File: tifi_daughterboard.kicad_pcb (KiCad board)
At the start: 2 copper layers, 57.4 x 32.3 mm, 19 parts, among them J1 SSW-110-23-F-D, J2 SSW-110-23-F-D, J3 SM04B-SRSS-TB(LF)(SN), J4 SSW-103-02-T-S-RA, Q1 BSS138LT1G, U1 SGP40-D-R4, U2 SHT40-AD1B-R3

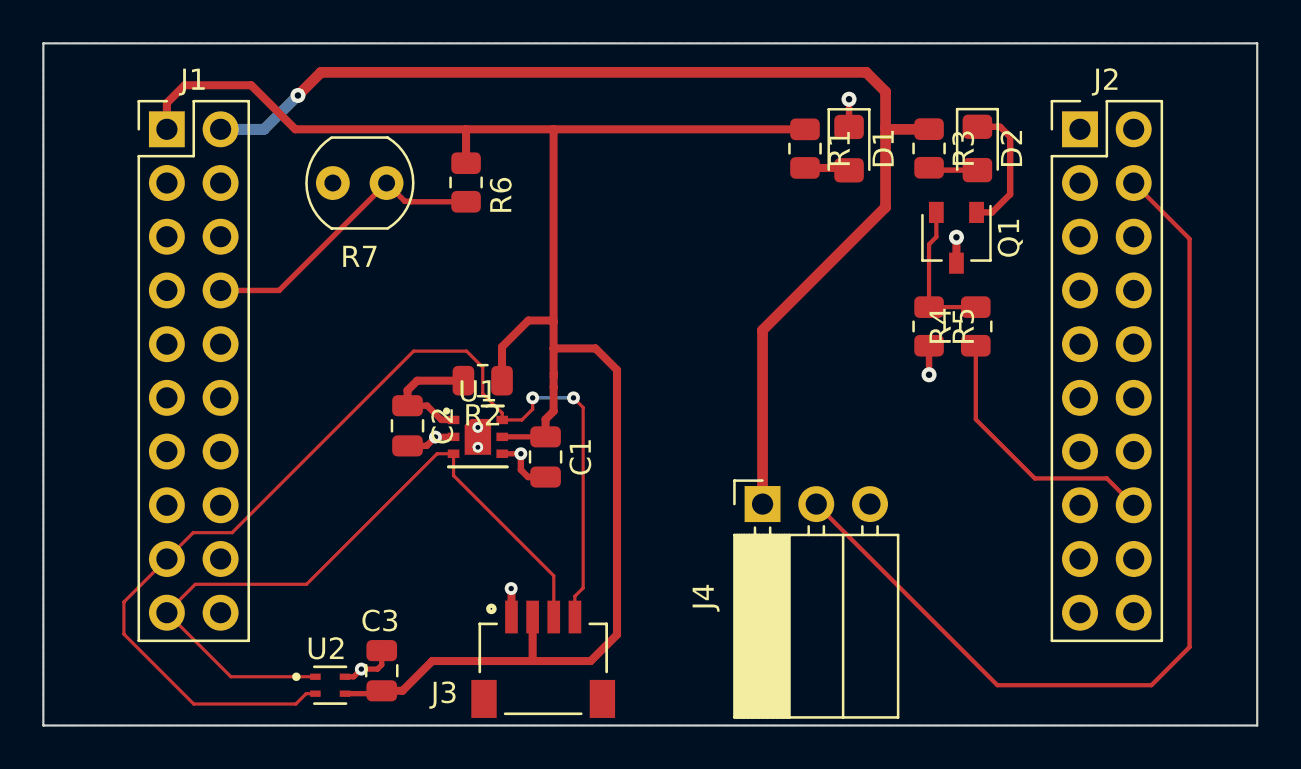
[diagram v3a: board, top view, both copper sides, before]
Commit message: Add alignment silkscreen.
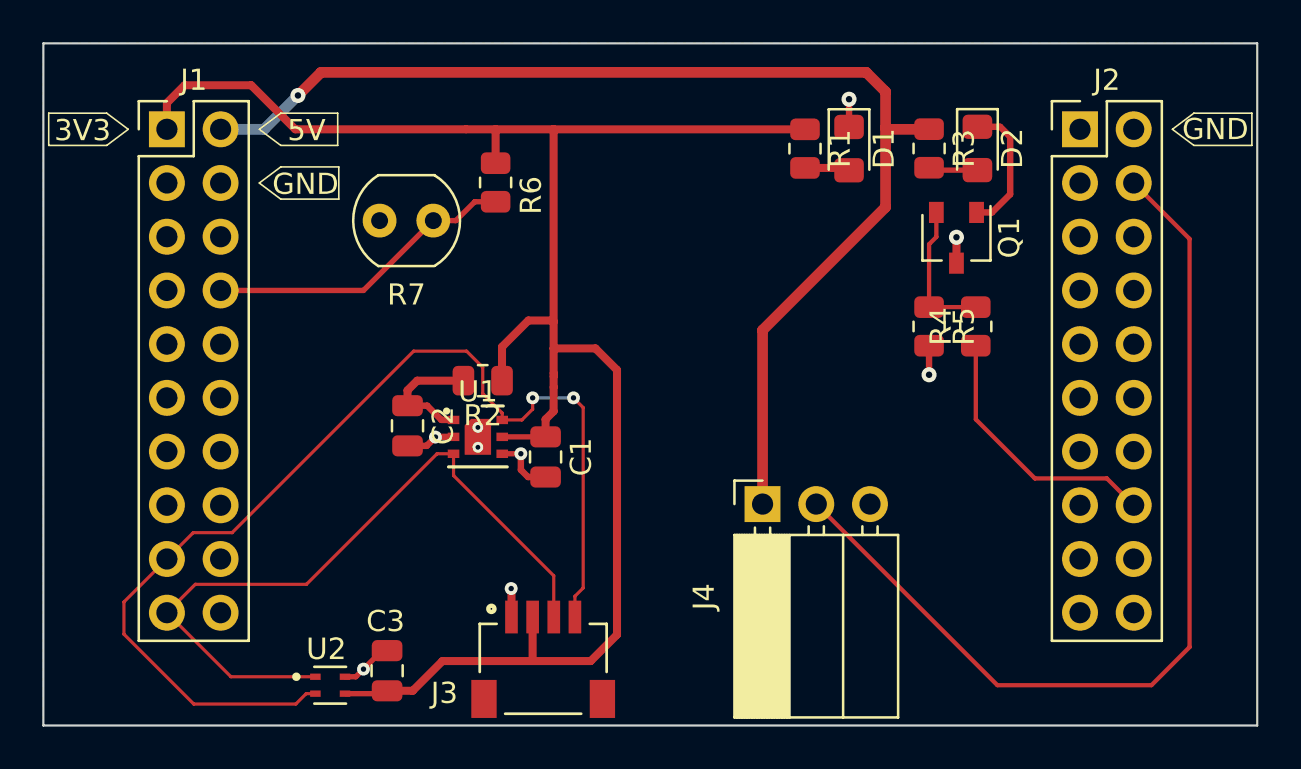
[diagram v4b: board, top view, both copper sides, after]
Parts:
- moved R7 2.84 mm to (134.5, 78.0)
- moved R6 1.40 mm to (137.5, 76.2)
- moved C3 0.25 mm to (132.3, 99.3)
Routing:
- net LDR_OUT: track 14.1 -> 14.7 mm
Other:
- board text added: "3V3"
- board text added: "5V"
- board text added: "GND"
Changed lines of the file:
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@@
     )
     (pad_to_mask_clearance 0)
+    (grid_origin 133.5532 99.822)
     (pcbplotparams
       (layerselection 0x00010fc_ffffffff)
@@
   )
   (footprint "OptoDevice:R_LDR_4.9x4.2mm_P2.54mm_Vertical" (layer "F.Cu")
-    (at 132.3086 76.2 180)
+    (at 134.5184 77.978 180)
     (descr "Resistor, LDR 4.9x4.2mm")
     (tags "Resistor LDR4.9x4.2")
@@
   )
   (footprint "Capacitor_SMD:C_0805_2012Metric" (layer "F.Cu")
-    (at 132.08 99.2632 90)
+    (at 132.334 99.2632 90)
     (descr "Capacitor SMD 0805 (2012 Metric), square (rectangular) end terminal, IPC_7351 nominal, (Body size source: IPC-SM-782 page 76, https://www.pcb-3d.com/wordpress/wp-content/uploads/ipc-sm-782a_amendment_1_and_2.pdf, https://docs.google.com/spreadsheets/d/1BsfQQcO9C6DZCsRaXUlFlo91Tg2WpOkGARC1WS5S8t0/edit?usp=sharing), generated with kicad-footprint-generator")
     (tags "capacitor")
@@
   )
   (footprint "Resistor_SMD:R_0805_2012Metric" (layer "F.Cu")
-    (at 136.0678 76.1746 -90)
+    (at 137.4648 76.1746 -90)
     (descr "Resistor SMD 0805 (2012 Metric), square (rectangular) end terminal, IPC_7351 nominal, (Body size source: IPC-SM-782 page 72, https://www.pcb-3d.com/wordpress/wp-content/uploads/ipc-sm-782a_amendment_1_and_2.pdf), generated with kicad-footprint-generator")
     (tags "resistor")
@@
     )
   )
+  (gr_poly
+    (pts
+      (xy 120.0912 73.66)
+      (xy 119.0752 74.422)
+      (xy 116.332 74.422)
+      (xy 116.332 72.898)
+      (xy 119.0752 72.898)
+    ) (layer "F.SilkS") (width 0.0762) (fill none))
+  (gr_poly
+    (pts
+      (xy 169.4688 73.66)
+      (xy 170.4848 72.898)
+      (xy 173.228 72.898)
+      (xy 173.228 74.422)
+      (xy 170.4848 74.422)
+    ) (layer "F.SilkS") (width 0.0762) (fill none))
+  (gr_poly
+    (pts
+      (xy 126.2888 76.2)
+      (xy 127.3048 75.438)
+      (xy 130.048 75.438)
+      (xy 130.048 76.962)
+      (xy 127.3048 76.962)
+    ) (layer "F.SilkS") (width 0.0762) (fill none))
+  (gr_poly
+    (pts
+      (xy 126.2888 73.66)
+      (xy 127.3048 72.898)
+      (xy 129.9972 72.898)
+      (xy 129.9972 74.422)
+      (xy 127.3048 74.422)
+    ) (layer "F.SilkS") (width 0.0762) (fill none))
   (gr_rect (start 116.078 69.596) (end 173.482 101.854) (layer "Edge.Cuts") (width 0.1016) (fill none))
-  (segment (start 139.2682 98.806) (end 134.4676 98.806) (width 0.381) (layer "F.Cu") (net 1))
+  (gr_text "GND" (at 128.4732 76.2508) (layer "F.SilkS")
+    (effects (font (size 1 1) (thickness 0.15)))
+  )
+  (gr_text "GND" (at 171.5008 73.66) (layer "F.SilkS")
+    (effects (font (size 1 1) (thickness 0.15)))
+  )
+  (gr_text "3V3" (at 117.9322 73.7108) (layer "F.SilkS")
+    (effects (font (size 1 1) (thickness 0.15)))
+  )
+  (gr_text "5V" (at 128.524 73.7108) (layer "F.SilkS")
+    (effects (font (size 1 1) (thickness 0.15)))
+  )
   (segment (start 140.208 85.852) (end 140.208 86.995) (width 0.381) (layer "F.Cu") (net 1))
   (segment (start 137.7677 85.5472) (end 137.7677 83.9489) (width 0.381) (layer "F.Cu") (net 1))
@@
   (segment (start 139.827 87.376) (end 139.827 88.204) (width 0.381) (layer "F.Cu") (net 1))
   (segment (start 139.2682 98.806) (end 139.215 98.7528) (width 0.381) (layer "F.Cu") (net 1))
-  (segment (start 136.0678 75.2621) (end 136.0678 73.66) (width 0.381) (layer "F.Cu") (net 1))
   (segment (start 139.215 98.7528) (end 139.215 96.7232) (width 0.381) (layer "F.Cu") (net 1))
+  (segment (start 140.208 73.66) (end 137.4648 73.66) (width 0.381) (layer "F.Cu") (net 1))
   (segment (start 139.0142 82.7024) (end 140.1572 82.7024) (width 0.381) (layer "F.Cu") (net 1))
+  (segment (start 137.4648 73.66) (end 136.0678 73.66) (width 0.381) (layer "F.Cu") (net 1))
   (segment (start 143.2052 97.5614) (end 141.9606 98.806) (width 0.381) (layer "F.Cu") (net 1))
-  (segment (start 133.0604 100.2132) (end 132.08 100.2132) (width 0.381) (layer "F.Cu") (net 1))
   (segment (start 140.208 84.0232) (end 142.1892 84.0232) (width 0.381) (layer "F.Cu") (net 1))
-  (segment (start 131.9442 100.349) (end 132.08 100.2132) (width 0.254) (layer "F.Cu") (net 1))
+  (segment (start 132.1322 100.349) (end 132.268 100.2132) (width 0.254) (layer "F.Cu") (net 1))
+  (segment (start 134.9502 98.806) (end 139.2682 98.806) (width 0.381) (layer "F.Cu") (net 1))
+  (segment (start 137.4648 75.2621) (end 137.4648 73.66) (width 0.381) (layer "F.Cu") (net 1))
   (segment (start 127.9906 73.66) (end 136.0678 73.66) (width 0.381) (layer "F.Cu") (net 1))
   (segment (start 142.1892 84.0232) (end 143.2052 85.0392) (width 0.381) (layer "F.Cu") (net 1))
   (segment (start 137.7677 83.9489) (end 139.0142 82.7024) (width 0.381) (layer "F.Cu") (net 1))
   (segment (start 140.208 85.344) (end 140.208 85.852) (width 0.381) (layer "F.Cu") (net 1))
+  (segment (start 133.543 100.2132) (end 134.9502 98.806) (width 0.381) (layer "F.Cu") (net 1))
   (segment (start 121.92 73.66) (end 121.92 72.4154) (width 0.381) (layer "F.Cu") (net 1))
+  (segment (start 132.268 100.2132) (end 133.543 100.2132) (width 0.381) (layer "F.Cu") (net 1))
   (segment (start 140.208 85.1916) (end 140.208 85.344) (width 0.381) (layer "F.Cu") (net 1))
   (segment (start 140.208 84.0232) (end 140.208 85.1916) (width 0.381) (layer "F.Cu") (net 1))
@@
   (segment (start 143.2052 85.0392) (end 143.2052 97.5614) (width 0.381) (layer "F.Cu") (net 1))
   (segment (start 137.7766 88.204) (end 139.827 88.204) (width 0.254) (layer "F.Cu") (net 1))
-  (segment (start 140.208 73.66) (end 136.0678 73.66) (width 0.381) (layer "F.Cu") (net 1))
   (segment (start 130.3416 100.349) (end 131.9442 100.349) (width 0.254) (layer "F.Cu") (net 1))
   (segment (start 140.2095 73.6615) (end 140.208 73.66) (width 0.381) (layer "F.Cu") (net 1))
   (segment (start 140.208 86.995) (end 139.827 87.376) (width 0.381) (layer "F.Cu") (net 1))
-  (segment (start 134.4676 98.806) (end 133.0604 100.2132) (width 0.381) (layer "F.Cu") (net 1))
   (segment (start 140.208 82.7532) (end 140.208 73.66) (width 0.381) (layer "F.Cu") (net 1))
   (segment (start 138.215 95.4668) (end 138.215 96.7232) (width 0.381) (layer "F.Cu") (net 2))
   (segment (start 137.7766 89.004) (end 138.6562 89.004) (width 0.254) (layer "F.Cu") (net 2))
   (segment (start 134.6302 88.204) (end 134.62 88.2142) (width 0.3048) (layer "F.Cu") (net 2))
-  (segment (start 131.1148 99.187) (end 131.8768 99.187) (width 0.254) (layer "F.Cu") (net 2))
   (segment (start 138.6586 89.7636) (end 138.999 90.104) (width 0.3048) (layer "F.Cu") (net 2))
-  (segment (start 131.8768 99.187) (end 132.08 98.9838) (width 0.254) (layer "F.Cu") (net 2))
+  (segment (start 130.8544 99.549) (end 130.3416 99.549) (width 0.254) (layer "F.Cu") (net 2))
   (segment (start 138.2014 95.4532) (end 138.215 95.4668) (width 0.381) (layer "F.Cu") (net 2))
   (segment (start 138.6562 89.004) (end 138.6586 89.0016) (width 0.254) (layer "F.Cu") (net 2))
-  (segment (start 130.7528 99.549) (end 131.1148 99.187) (width 0.254) (layer "F.Cu") (net 2))
-  (segment (start 130.3416 99.549) (end 130.7528 99.549) (width 0.254) (layer "F.Cu") (net 2))
+  (segment (start 131.2164 99.187) (end 130.8544 99.549) (width 0.254) (layer "F.Cu") (net 2))
   (segment (start 159.258 78.7654) (end 159.258 79.9908) (width 0.381) (layer "F.Cu") (net 2))
   (segment (start 157.9626 85.2678) (end 157.9626 83.8943) (width 0.3048) (layer "F.Cu") (net 2))
   (segment (start 135.4766 88.204) (end 134.6302 88.204) (width 0.3048) (layer "F.Cu") (net 2))
+  (segment (start 132.334 98.3132) (end 132.0902 98.3132) (width 0.254) (layer "F.Cu") (net 2))
   (segment (start 138.999 90.104) (end 139.827 90.104) (width 0.3048) (layer "F.Cu") (net 2))
   (segment (start 134.2034 88.6308) (end 134.62 88.2142) (width 0.3048) (layer "F.Cu") (net 2))
@@
   (segment (start 138.6586 89.0016) (end 138.6586 89.7636) (width 0.3048) (layer "F.Cu") (net 2))
   (segment (start 133.2992 88.6308) (end 134.2034 88.6308) (width 0.3048) (layer "F.Cu") (net 2))
-  (segment (start 132.08 98.9838) (end 132.08 98.3132) (width 0.254) (layer "F.Cu") (net 2))
-  (via (at 131.1148 99.187) (size 0.6096) (drill 0.254) (layers "F.Cu" "B.Cu") (free) (net 2))
+  (segment (start 132.0902 98.3132) (end 131.2164 99.187) (width 0.254) (layer "F.Cu") (net 2))
+  (via (at 131.2164 99.187) (size 0.6096) (drill 0.254) (layers "F.Cu" "B.Cu") (free) (net 2))
   (via (at 154.178 72.2376) (size 0.7112) (drill 0.3048) (layers "F.Cu" "B.Cu") (free) (net 2))
   (via (at 157.9626 85.2678) (size 0.7112) (drill 0.3048) (layers "F.Cu" "B.Cu") (free) (net 2))
@@
   (segment (start 126.5174 73.66) (end 124.46 73.66) (width 0.508) (layer "B.Cu") (net 6))
   (segment (start 128.1176 72.0598) (end 126.5174 73.66) (width 0.508) (layer "B.Cu") (net 6))
-  (segment (start 132.3086 76.2) (end 127.2286 81.28) (width 0.254) (layer "F.Cu") (net 11))
-  (segment (start 136.0678 77.0871) (end 133.4497 77.0871) (width 0.254) (layer "F.Cu") (net 11))
-  (segment (start 133.1722 77.0636) (end 132.3086 76.2) (width 0.254) (layer "F.Cu") (net 11))
-  (segment (start 127.2286 81.28) (end 124.46 81.28) (width 0.254) (layer "F.Cu") (net 11))
-  (segment (start 133.4497 77.0871) (end 133.4262 77.0636) (width 0.254) (layer "F.Cu") (net 11))
-  (segment (start 133.4262 77.0636) (end 133.1722 77.0636) (width 0.254) (layer "F.Cu") (net 11))
+  (segment (start 136.4761 77.0871) (end 135.5852 77.978) (width 0.254) (layer "F.Cu") (net 11))
+  (segment (start 137.4648 77.0871) (end 136.4761 77.0871) (width 0.254) (layer "F.Cu") (net 11))
+  (segment (start 135.5852 77.978) (end 134.5184 77.978) (width 0.254) (layer "F.Cu") (net 11))
+  (segment (start 134.5184 77.978) (end 131.2164 81.28) (width 0.254) (layer "F.Cu") (net 11))
+  (segment (start 131.2164 81.28) (end 124.46 81.28) (width 0.254) (layer "F.Cu") (net 11))
   (segment (start 170.2816 98.1456) (end 170.2816 78.8416) (width 0.2032) (layer "F.Cu") (net 12))
   (segment (start 170.2816 78.8416) (end 167.64 76.2) (width 0.2032) (layer "F.Cu") (net 12))

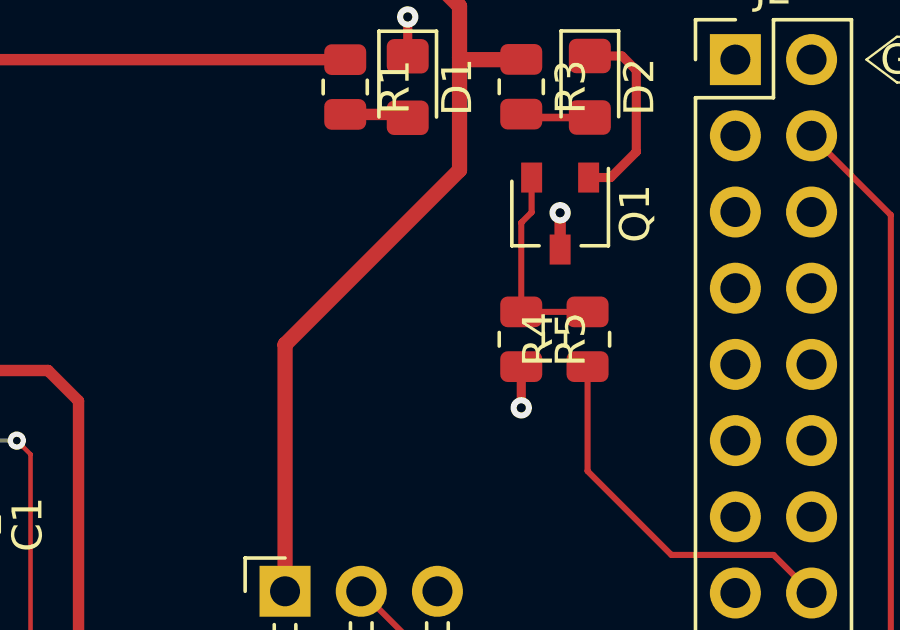
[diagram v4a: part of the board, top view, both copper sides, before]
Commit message: Add testpoint for LED driver FET gate.
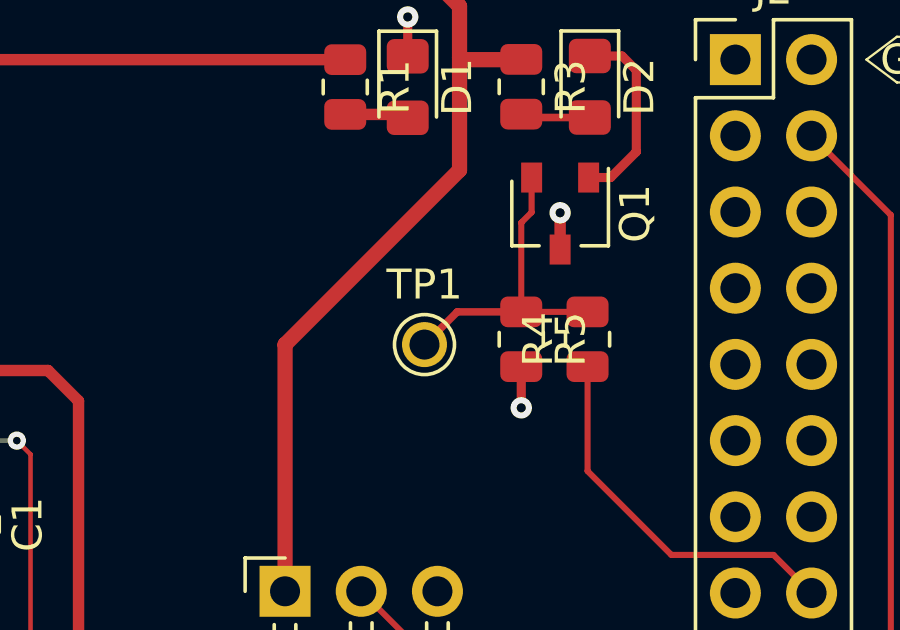
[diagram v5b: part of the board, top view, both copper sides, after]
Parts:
- added TP1: TestPoint, TiFi Footprints:TestPoint_THTPad_D1.5mm_Drill1.0mm, F.Cu at (154.7, 83.2)
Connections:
- U1 pad 7: GND -> (no net)
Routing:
- net Net-(Q1-Pad2): track 6.83 -> 10.5 mm
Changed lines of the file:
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@@
       (net 20 "I2C_SCL") (pinfunction "SCL") (pintype "input"))
     (pad "7" smd roundrect (at 0 0) (size 1.25 1.7) (layers "F.Cu" "F.Mask") (roundrect_rratio 0)
-      (chamfer_ratio 0.24) (chamfer top_left)
-      (net 2 "GND"))
+      (chamfer_ratio 0.24) (chamfer top_left))
     (model "${KICAD6_3DMODEL_DIR}/Package_DFN_QFN.3dshapes/DFN-6-1EP_2x2mm_P0.5mm_EP0.61x1.42mm.wrl" hide
       (offset (xyz 0 0 0))
@@
       (rotate (xyz -90 0 0))
     )
+  )
+  (footprint "TiFi Footprints:TestPoint_THTPad_D1.5mm_Drill1.0mm" (layer "F.Cu")
+    (at 154.7368 83.1596)
+    (descr "THT pad as test Point, diameter 2.0mm, hole diameter 1.0mm")
+    (tags "test point THT pad")
+    (property "Sheetfile" "tifi_daughterboard.kicad_sch")
+    (property "Sheetname" "")
+    (attr exclude_from_pos_files)
+    (fp_text reference "TP1" (at 0 -1.998) (layer "F.SilkS")
+      (effects (font (size 1 1) (thickness 0.15)))
+    )
+    (fp_text value "TestPoint" (at 0 2.05) (layer "F.Fab")
+      (effects (font (size 1 1) (thickness 0.15)))
+    )
+    (fp_text user "${REFERENCE}" (at 0 -2) (layer "F.Fab")
+      (effects (font (size 1 1) (thickness 0.15)))
+    )
+    (fp_circle (center 0 0) (end 1 0) (layer "F.SilkS") (width 0.12) (fill none))
+    (fp_circle (center 0 0) (end 1.3 0) (layer "F.CrtYd") (width 0.05) (fill none))
+    (pad "1" thru_hole circle (at 0 0) (size 1.5 1.5) (drill 1) (layers *.Cu *.Mask)
+      (net 42 "Net-(Q1-Pad2)") (pinfunction "1") (pintype "passive"))
   )
   (footprint "Capacitor_SMD:C_0805_2012Metric" (layer "F.Cu")
@@
   (segment (start 162.9664 90.17) (end 160.1724 87.376) (width 0.2032) (layer "F.Cu") (net 37))
   (segment (start 157.9626 79.0956) (end 158.308 78.7502) (width 0.2032) (layer "F.Cu") (net 42))
+  (segment (start 155.8271 82.0693) (end 157.9626 82.0693) (width 0.25) (layer "F.Cu") (net 42))
+  (segment (start 154.7368 83.1596) (end 155.8271 82.0693) (width 0.25) (layer "F.Cu") (net 42))
   (segment (start 160.1724 82.0693) (end 157.9626 82.0693) (width 0.2032) (layer "F.Cu") (net 42))
   (segment (start 157.9626 82.0693) (end 157.9626 79.0956) (width 0.2032) (layer "F.Cu") (net 42))
